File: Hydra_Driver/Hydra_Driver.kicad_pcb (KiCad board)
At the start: 2 copper layers, 59.2 x 42 mm, 88 parts, among them IC1 ESP32-S3-WROOM-1-N4, IC2 DRV8313RHHR, IC3 DRV8313RHHR, J1 USB4105-GF-A, J10 Conn_01x03, J11 Conn_01x04, J12 Conn_01x03, J13 Conn_01x02, J2 Conn_01x02, J3 Conn_01x06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

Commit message: Consolidated pullup resistors to 10k
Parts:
- R12, R13, R14, R16, R19, R20, R21, R23: value 3.3k -> 10k

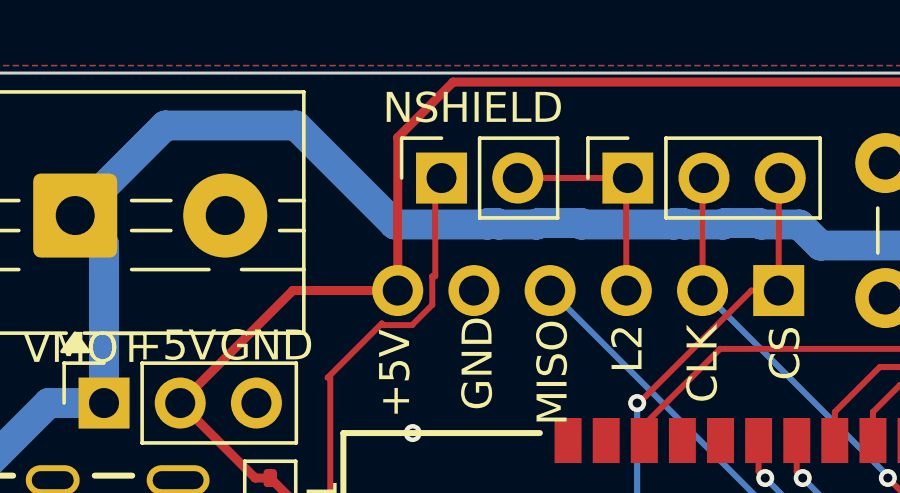
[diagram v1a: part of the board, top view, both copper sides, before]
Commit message: Changed shield passthrough to pin header
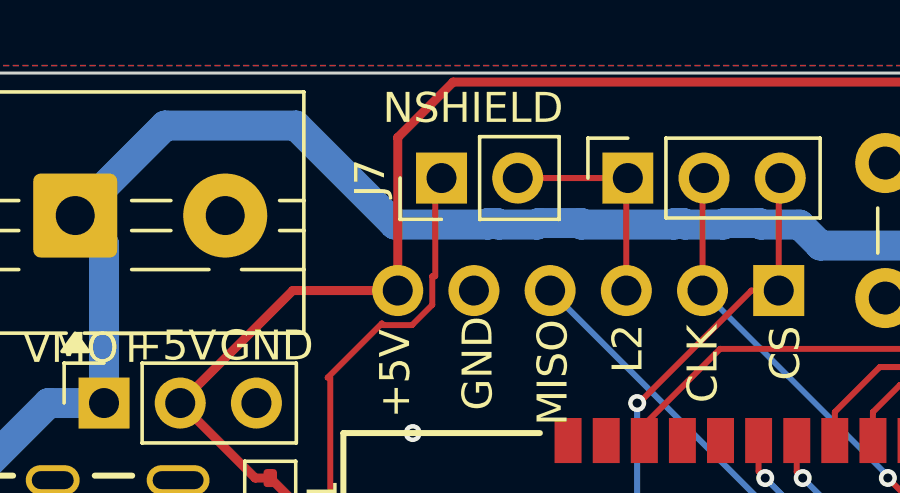
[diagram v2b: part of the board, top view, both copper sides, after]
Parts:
- J7: footprint Connector_PinSocket_2.54mm:PinSocket_1x02_P2.54mm_Vertical -> Connector_PinHeader_2.54mm:PinHeader_1x02_P2.54mm_Vertical
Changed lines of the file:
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@@
 		)
 	)
-	(footprint "Connector_PinSocket_2.54mm:PinSocket_1x02_P2.54mm_Vertical"
+	(footprint "Connector_PinHeader_2.54mm:PinHeader_1x02_P2.54mm_Vertical"
 		(layer "F.Cu")
 		(at 15.96 3.5 90)
-		(descr "Through hole straight socket strip, 1x02, 2.54mm pitch, single row (from Kicad 4.0.7), script generated")
-		(tags "Through hole socket strip THT 1x02 2.54mm single row")
+		(descr "Through hole straight pin header, 1x02, 2.54mm pitch, single row")
+		(tags "Through hole pin header THT 1x02 2.54mm single row")
 		(property "Reference" "J7"
-			(at 0 -2.77 90)
-			(layer "F.SilkS")
-			(hide yes)
+			(at 0 -2.38 90)
+			(layer "F.SilkS")
 			(effects
 				(font
@@
 		)
 		(property "Value" "Conn_01x02"
-			(at 0 5.31 90)
+			(at 0 4.92 90)
 			(layer "F.Fab")
 			(effects
@@
 		(attr through_hole)
 		(fp_line
-			(start 1.33 -1.33)
-			(end 1.33 0)
-			(stroke
-				(width 0.12)
-				(type solid)
-			)
-			(layer "F.SilkS")
-		)
-		(fp_line
-			(start 0 -1.33)
-			(end 1.33 -1.33)
-			(stroke
-				(width 0.12)
-				(type solid)
-			)
-			(layer "F.SilkS")
-		)
-		(fp_line
-			(start 1.33 1.27)
-			(end 1.33 3.87)
-			(stroke
-				(width 0.12)
-				(type solid)
-			)
-			(layer "F.SilkS")
-		)
-		(fp_line
-			(start -1.33 1.27)
-			(end 1.33 1.27)
-			(stroke
-				(width 0.12)
-				(type solid)
-			)
-			(layer "F.SilkS")
-		)
-		(fp_line
-			(start -1.33 1.27)
-			(end -1.33 3.87)
-			(stroke
-				(width 0.12)
-				(type solid)
-			)
-			(layer "F.SilkS")
-		)
-		(fp_line
-			(start -1.33 3.87)
-			(end 1.33 3.87)
-			(stroke
-				(width 0.12)
-				(type solid)
-			)
-			(layer "F.SilkS")
-		)
-		(fp_line
-			(start 1.75 -1.8)
-			(end 1.75 4.3)
-			(stroke
-				(width 0.05)
-				(type solid)
-			)
-			(layer "F.CrtYd")
-		)
-		(fp_line
-			(start -1.8 -1.8)
-			(end 1.75 -1.8)
-			(stroke
-				(width 0.05)
-				(type solid)
-			)
-			(layer "F.CrtYd")
-		)
-		(fp_line
-			(start 1.75 4.3)
-			(end -1.8 4.3)
-			(stroke
-				(width 0.05)
-				(type solid)
-			)
-			(layer "F.CrtYd")
-		)
-		(fp_line
-			(start -1.8 4.3)
-			(end -1.8 -1.8)
-			(stroke
-				(width 0.05)
-				(type solid)
-			)
-			(layer "F.CrtYd")
-		)
-		(fp_line
-			(start 0.635 -1.27)
-			(end 1.27 -0.635)
-			(stroke
-				(width 0.1)
-				(type solid)
-			)
-			(layer "F.Fab")
-		)
-		(fp_line
-			(start -1.27 -1.27)
-			(end 0.635 -1.27)
-			(stroke
-				(width 0.1)
-				(type solid)
-			)
-			(layer "F.Fab")
-		)
-		(fp_line
-			(start 1.27 -0.635)
+			(start -1.38 -1.38)
+			(end 0 -1.38)
+			(stroke
+				(width 0.12)
+				(type solid)
+			)
+			(layer "F.SilkS")
+		)
+		(fp_line
+			(start -1.38 0)
+			(end -1.38 -1.38)
+			(stroke
+				(width 0.12)
+				(type solid)
+			)
+			(layer "F.SilkS")
+		)
+		(fp_line
+			(start 1.38 1.27)
+			(end 1.38 3.92)
+			(stroke
+				(width 0.12)
+				(type solid)
+			)
+			(layer "F.SilkS")
+		)
+		(fp_line
+			(start -1.38 1.27)
+			(end 1.38 1.27)
+			(stroke
+				(width 0.12)
+				(type solid)
+			)
+			(layer "F.SilkS")
+		)
+		(fp_line
+			(start -1.38 1.27)
+			(end -1.38 3.92)
+			(stroke
+				(width 0.12)
+				(type solid)
+			)
+			(layer "F.SilkS")
+		)
+		(fp_line
+			(start -1.38 3.92)
+			(end 1.38 3.92)
+			(stroke
+				(width 0.12)
+				(type solid)
+			)
+			(layer "F.SilkS")
+		)
+		(fp_line
+			(start 1.77 -1.77)
+			(end -1.77 -1.77)
+			(stroke
+				(width 0.05)
+				(type solid)
+			)
+			(layer "F.CrtYd")
+		)
+		(fp_line
+			(start -1.77 -1.77)
+			(end -1.77 4.32)
+			(stroke
+				(width 0.05)
+				(type solid)
+			)
+			(layer "F.CrtYd")
+		)
+		(fp_line
+			(start 1.77 4.32)
+			(end 1.77 -1.77)
+			(stroke
+				(width 0.05)
+				(type solid)
+			)
+			(layer "F.CrtYd")
+		)
+		(fp_line
+			(start -1.77 4.32)
+			(end 1.77 4.32)
+			(stroke
+				(width 0.05)
+				(type solid)
+			)
+			(layer "F.CrtYd")
+		)
+		(fp_line
+			(start 1.27 -1.27)
 			(end 1.27 3.81)
+			(stroke
+				(width 0.1)
+				(type solid)
+			)
+			(layer "F.Fab")
+		)
+		(fp_line
+			(start -0.635 -1.27)
+			(end 1.27 -1.27)
+			(stroke
+				(width 0.1)
+				(type solid)
+			)
+			(layer "F.Fab")
+		)
+		(fp_line
+			(start -1.27 -0.635)
+			(end -0.635 -1.27)
 			(stroke
 				(width 0.1)
@@
 		(fp_line
 			(start -1.27 3.81)
-			(end -1.27 -1.27)
+			(end -1.27 -0.635)
 			(stroke
 				(width 0.1)
@@
 		)
 		(fp_text user "${REFERENCE}"
-			(at 0 1.27 0)
+			(at 0 1.27 180)
 			(layer "F.Fab")
 			(effects
@@
 		)
 		(embedded_fonts no)
-		(model "${KICAD9_3DMODEL_DIR}/Connector_PinSocket_2.54mm.3dshapes/PinSocket_1x02_P2.54mm_Vertical.step"
+		(model "${KICAD9_3DMODEL_DIR}/Connector_PinHeader_2.54mm.3dshapes/PinHeader_1x02_P2.54mm_Vertical.step"
 			(offset
 				(xyz 0 0 0)
